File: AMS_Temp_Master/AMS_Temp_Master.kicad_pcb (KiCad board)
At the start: 2 copper layers, 36 parts, among them J1 Conn_01x10_Socket, J2 Conn_01x02_Pin, J3 Conn_01x02_Pin, J4 Conn_01x04_Pin, J5 Conn_01x02_Pin, U1 ATmega328P-A, U2 MCP2515-xSO, U3 MCP2551-I-SN, U4 LD1117S50TR_SOT223, Y1 CSTCE16M0V53-R0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

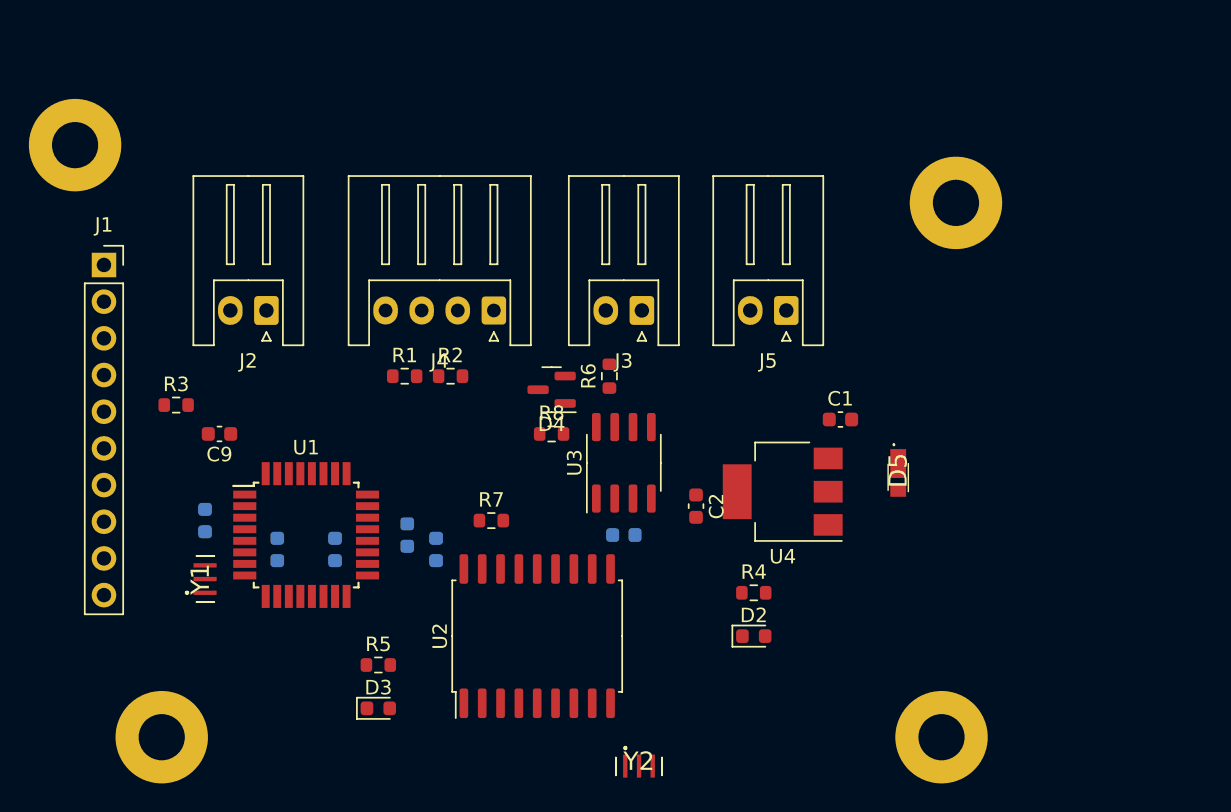
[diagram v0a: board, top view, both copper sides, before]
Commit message: 回路図修正, パターン作成
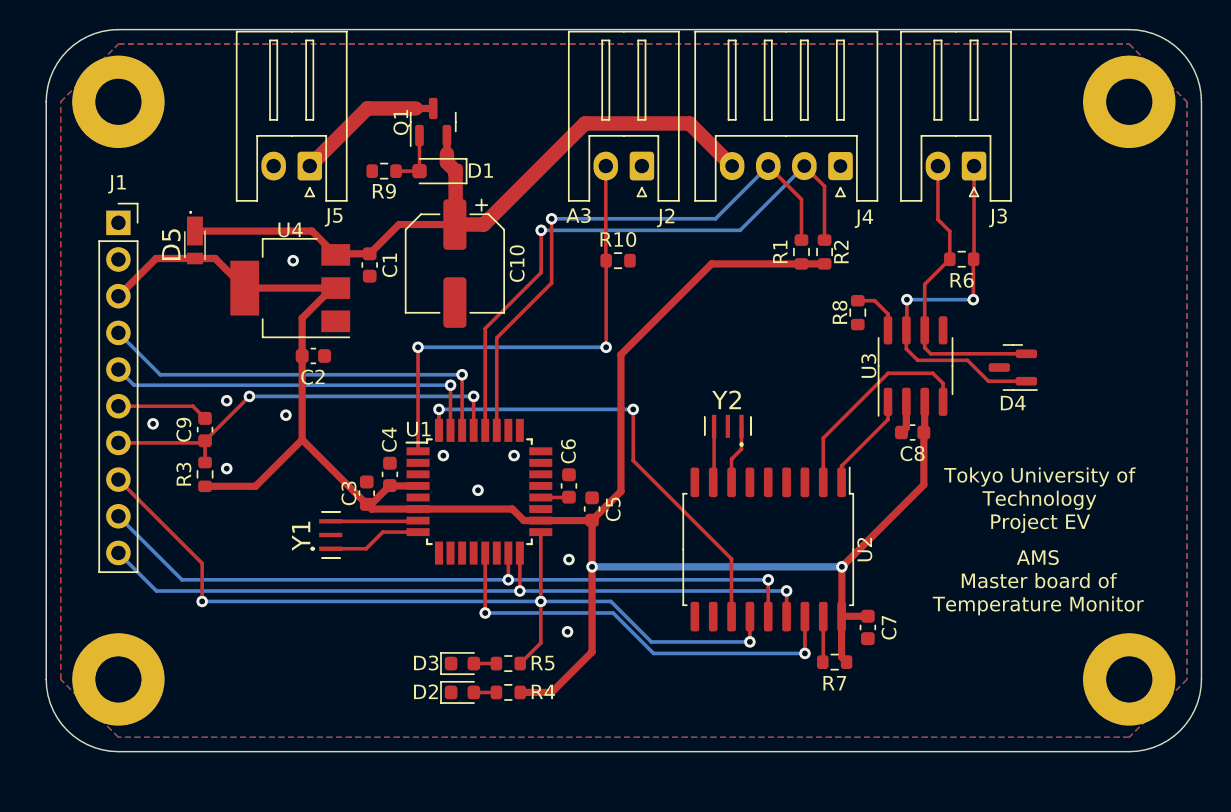
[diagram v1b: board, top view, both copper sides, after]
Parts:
- added C10: 470u, Capacitor_SMD:CP_Elec_6.3x5.4_Nichicon, F.Cu at (138.3, 86.2)
- added D1: UDZV5.1B, Diode_SMD:D_SOD-323_HandSoldering, F.Cu at (137.1, 79.8)
- added Q1: AO3401A, Package_TO_SOT_SMD:SOT-23, F.Cu at (136.8, 76.4)
- added R10: 10k, Resistor_SMD:R_0603_1608Metric, F.Cu at (149.6, 86.0)
- added R9: 10k, Resistor_SMD:R_0603_1608Metric, F.Cu at (133.4, 79.8)
- C3, C4, C5, C6, C7, C8: moved to F.Cu
- moved D5 51.3 mm to (120.3, 84.9)
- moved U4 36.9 mm to (126.9, 87.9)
- moved J5 34.5 mm to (128.2, 79.5)
- moved C1 34.3 mm to (132.4, 86.3), turned to -90 degrees
- moved D4 32.0 mm to (176.9, 93.4)
- moved C7 30.4 mm to (166.9, 111.4), turned to -90 degrees
- moved R1 28.8 mm to (162.3, 85.4), turned to 90 degrees
- moved C2 28.5 mm to (128.5, 92.6), turned to 0 degrees
- moved J2 27.9 mm to (151.2, 79.5)
- moved R2 27.3 mm to (163.9, 85.4), turned to 90 degrees
- moved J4 26.0 mm to (165.0, 79.5)
- moved R7 25.7 mm to (164.6, 113.8), turned to 180 degrees
- moved R6 25.7 mm to (173.4, 85.9), turned to 180 degrees
- moved J3 25.1 mm to (174.2, 79.5)
- moved Y2 24.3 mm to (157.2, 97.5), turned to 0 degrees
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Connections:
- net Net-(J1-Pin_6) renamed /DTR
- net Net-(U1-AREF) renamed /AREF
- net Net-(U1-XTAL1/PB6) renamed /XTAL1
- net Net-(U1-XTAL2/PB7) renamed /XTAL2
- J5 pad 1: +12V -> /+12Vin
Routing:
- net VCC: track 0.00 -> 147.1 mm, vias 0 -> 2
- net /SCK: track 0.00 -> 61.7 mm, vias 0 -> 3
- net /MISO: track 0.00 -> 51.8 mm, vias 0 -> 2
- net /MOSI: track 0.00 -> 51.2 mm, vias 0 -> 2
- net +12V: track 0.00 -> 49.3 mm
- net /SCL: track 0.00 -> 41.2 mm, vias 0 -> 1
- net /SDA: track 0.00 -> 38.8 mm, vias 0 -> 1
- net /AMS_SIG: track 0.00 -> 32.8 mm, vias 0 -> 2
- net /INT: track 0.00 -> 32.1 mm, vias 0 -> 2
- net /CS: track 0.00 -> 30.0 mm, vias 0 -> 2
- net /RESET1: track 0.00 -> 29.8 mm, vias 0 -> 2
- net /RXI: track 0.00 -> 28.9 mm, vias 0 -> 1
- net /TXO: track 0.00 -> 26.6 mm, vias 0 -> 1
- net /CANH: track 0.00 -> 26.5 mm, vias 0 -> 2
- net /CANL: track 0.00 -> 20.9 mm
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- added copper zone on B.Cu, net GND
- added copper zone on F.Cu, net GND
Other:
- board outline added: 80 x 50 mm
- board text added: "A3"
- board text added: "AMS Master board of Temperature Monitor"
- board text added: "Tokyo University of Technology Project EV"

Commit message: パターン作成
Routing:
- net GND: track 2.27 -> 12.6 mm, vias 10 -> 212

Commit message: 修正とパターン完成
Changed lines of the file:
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@@
   (via (at 136.5 90.7) (size 0.8) (drill 0.4) (layers "F.Cu" "B.Cu") (free) (net 2))
   (via (at 153.2 78.2) (size 0.8) (drill 0.4) (layers "F.Cu" "B.Cu") (free) (net 2))
-  (via (at 153.4 100.7) (size 0.8) (drill 0.4) (layers "F.Cu" "B.Cu") (free) (net 2))
+  (via (at 153.6 101.1) (size 0.8) (drill 0.4) (layers "F.Cu" "B.Cu") (free) (net 2))
   (via (at 143 88.1) (size 0.8) (drill 0.4) (layers "F.Cu" "B.Cu") (free) (net 2))
-  (via (at 173.5 94.2) (size 0.8) (drill 0.4) (layers "F.Cu" "B.Cu") (free) (net 2))
+  (via (at 173.4 94.1) (size 0.8) (drill 0.4) (layers "F.Cu" "B.Cu") (free) (net 2))
   (via (at 119.7 102.8) (size 0.8) (drill 0.4) (layers "F.Cu" "B.Cu") (free) (net 2))
   (via (at 148.5 100.9) (size 0.8) (drill 0.4) (layers "F.Cu" "B.Cu") (free) (net 2))
@@
   (via (at 144.1 97.8) (size 0.8) (drill 0.4) (layers "F.Cu" "B.Cu") (free) (net 2))
   (via (at 156.1 118.1) (size 0.8) (drill 0.4) (layers "F.Cu" "B.Cu") (free) (net 2))
-  (via (at 165.1 95.2) (size 0.8) (drill 0.4) (layers "F.Cu" "B.Cu") (free) (net 2))
+  (via (at 164.8 94.8) (size 0.8) (drill 0.4) (layers "F.Cu" "B.Cu") (free) (net 2))
   (via (at 181.9 118.4) (size 0.8) (drill 0.4) (layers "F.Cu" "B.Cu") (free) (net 2))
   (via (at 148.6 94.5) (size 0.8) (drill 0.4) (layers "F.Cu" "B.Cu") (free) (net 2))
@@
   (via (at 116.9 97.4) (size 0.8) (drill 0.4) (layers "F.Cu" "B.Cu") (free) (net 2))
   (via (at 158.8 72) (size 0.8) (drill 0.4) (layers "F.Cu" "B.Cu") (free) (net 2))
-  (via (at 168.1 99.1) (size 0.8) (drill 0.4) (layers "F.Cu" "B.Cu") (free) (net 2))
+  (via (at 168 98.9) (size 0.8) (drill 0.4) (layers "F.Cu" "B.Cu") (free) (net 2))
   (via (at 121.7 87.8) (size 0.8) (drill 0.4) (layers "F.Cu" "B.Cu") (free) (net 2))
   (via (at 183.7 93.5) (size 0.8) (drill 0.4) (layers "F.Cu" "B.Cu") (free) (net 2))
@@
   (segment (start 168.295 95.775) (end 168.295 97.005) (width 0.25) (layer "F.Cu") (net 35))
   (segment (start 168.295 97.005) (end 165.08 100.22) (width 0.25) (layer "F.Cu") (net 35))
-  (segment (start 163.81 98.29) (end 168.3 93.8) (width 0.25) (layer "F.Cu") (net 36))
-  (segment (start 163.81 101.35) (end 163.81 98.29) (width 0.25) (layer "F.Cu") (net 36))
+  (segment (start 167.5 93.8) (end 171.4 93.8) (width 0.25) (layer "F.Cu") (net 36))
   (segment (start 171.4 93.8) (end 172.105 94.505) (width 0.25) (layer "F.Cu") (net 36))
+  (segment (start 163.81 101.35) (end 163.81 97.49) (width 0.25) (layer "F.Cu") (net 36))
+  (segment (start 163.81 97.49) (end 167.5 93.8) (width 0.25) (layer "F.Cu") (net 36))
   (segment (start 172.105 94.505) (end 172.105 95.775) (width 0.25) (layer "F.Cu") (net 36))
-  (segment (start 168.3 93.8) (end 171.4 93.8) (width 0.25) (layer "F.Cu") (net 36))
   (segment (start 157.46 99.14) (end 157.46 101.35) (width 0.25) (layer "F.Cu") (net 41))
   (segment (start 158.15 98.45) (end 157.46 99.14) (width 0.25) (layer "F.Cu") (net 41))

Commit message: modify and complete
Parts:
- moved R8 2.01 mm to (166.4, 91.6)
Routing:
- net /Rs: track 3.61 -> 1.92 mm
- net VCC: track 147.1 -> 145.8 mm
- net GND: track 12.6 -> 12.9 mm, vias 212 -> 187

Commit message: 修正
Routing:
- net GND: vias 187 -> 189
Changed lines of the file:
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@@
   (via (at 149.1 105.8) (size 0.8) (drill 0.4) (layers "F.Cu" "B.Cu") (free) (net 2))
   (via (at 136.5 90.7) (size 0.8) (drill 0.4) (layers "F.Cu" "B.Cu") (free) (net 2))
-  (via (at 153.2 78.9) (size 0.8) (drill 0.4) (layers "F.Cu" "B.Cu") (free) (net 2))
+  (via (at 153.1 78.4) (size 0.8) (drill 0.4) (layers "F.Cu" "B.Cu") (free) (net 2))
   (via (at 153.4 100.7) (size 0.8) (drill 0.4) (layers "F.Cu" "B.Cu") (free) (net 2))
   (via (at 143 88.1) (size 0.8) (drill 0.4) (layers "F.Cu" "B.Cu") (free) (net 2))
@@
   (via (at 144.1 97.8) (size 0.8) (drill 0.4) (layers "F.Cu" "B.Cu") (free) (net 2))
   (via (at 156.1 118.1) (size 0.8) (drill 0.4) (layers "F.Cu" "B.Cu") (free) (net 2))
-  (via (at 164.8 94.8) (size 0.8) (drill 0.4) (layers "F.Cu" "B.Cu") (free) (net 2))
+  (via (at 165.8 93.8) (size 0.8) (drill 0.4) (layers "F.Cu" "B.Cu") (free) (net 2))
   (via (at 148.6 94.5) (size 0.8) (drill 0.4) (layers "F.Cu" "B.Cu") (free) (net 2))
   (via (at 183.6 80.4) (size 0.8) (drill 0.4) (layers "F.Cu" "B.Cu") (free) (net 2))
@@
   (via (at 179.2 73.7) (size 0.8) (drill 0.4) (layers "F.Cu" "B.Cu") (free) (net 2))
   (via (at 155.2 85.1) (size 0.8) (drill 0.4) (layers "F.Cu" "B.Cu") (free) (net 2))
-  (via (at 141.5 80.2) (size 0.8) (drill 0.4) (layers "F.Cu" "B.Cu") (free) (net 2))
+  (via (at 141.4 80.3) (size 0.8) (drill 0.4) (layers "F.Cu" "B.Cu") (free) (net 2))
   (via (at 162.6 99.2) (size 0.8) (drill 0.4) (layers "F.Cu" "B.Cu") (free) (net 2))
   (via (at 147.7 92) (size 0.8) (drill 0.4) (layers "F.Cu" "B.Cu") (free) (net 2))
@@
   (via (at 156.2 75.5) (size 0.8) (drill 0.4) (layers "F.Cu" "B.Cu") (free) (net 2))
   (via (at 153.4 111.2) (size 0.8) (drill 0.4) (layers "F.Cu" "B.Cu") (free) (net 2))
-  (via (at 151.3 110.1) (size 0.8) (drill 0.4) (layers "F.Cu" "B.Cu") (free) (net 2))
+  (via (at 151.7 110.1) (size 0.8) (drill 0.4) (layers "F.Cu" "B.Cu") (free) (net 2))
   (via (at 179.2 91.1) (size 0.8) (drill 0.4) (layers "F.Cu" "B.Cu") (free) (net 2))
   (via (at 150 87.5) (size 0.8) (drill 0.4) (layers "F.Cu" "B.Cu") (free) (net 2))
@@
   (via (at 145.5 95.2) (size 0.8) (drill 0.4) (layers "F.Cu" "B.Cu") (free) (net 2))
   (via (at 136.4 81.4) (size 0.8) (drill 0.4) (layers "F.Cu" "B.Cu") (free) (net 2))
-  (via (at 117 91.2) (size 0.8) (drill 0.4) (layers "F.Cu" "B.Cu") (free) (net 2))
+  (via (at 117.2 91.3) (size 0.8) (drill 0.4) (layers "F.Cu" "B.Cu") (free) (net 2))
   (via (at 126.6 106.7) (size 0.8) (drill 0.4) (layers "F.Cu" "B.Cu") (free) (net 2))
   (via (at 169.4 101) (size 0.8) (drill 0.4) (layers "F.Cu" "B.Cu") (free) (net 2))
@@
   (via (at 161.3 118) (size 0.8) (drill 0.4) (layers "F.Cu" "B.Cu") (free) (net 2))
   (via (at 118.6 71.7) (size 0.8) (drill 0.4) (layers "F.Cu" "B.Cu") (free) (net 2))
-  (via (at 174.6 97.8) (size 0.8) (drill 0.4) (layers "F.Cu" "B.Cu") (free) (net 2))
+  (via (at 173.4 95.7) (size 0.8) (drill 0.4) (layers "F.Cu" "B.Cu") (free) (net 2))
   (via (at 148.3 97.6) (size 0.8) (drill 0.4) (layers "F.Cu" "B.Cu") (free) (net 2))
   (via (at 161 95.2) (size 0.8) (drill 0.4) (layers "F.Cu" "B.Cu") (free) (net 2))
@@
   (via (at 148.4 114.6) (size 0.8) (drill 0.4) (layers "F.Cu" "B.Cu") (free) (net 2))
   (via (at 166.6 109.1) (size 0.8) (drill 0.4) (layers "F.Cu" "B.Cu") (free) (net 2))
-  (via (at 134.4 78.1) (size 0.8) (drill 0.4) (layers "F.Cu" "B.Cu") (free) (net 2))
+  (via (at 134.5 78.3) (size 0.8) (drill 0.4) (layers "F.Cu" "B.Cu") (free) (net 2))
   (via (at 160.7 84.8) (size 0.8) (drill 0.4) (layers "F.Cu" "B.Cu") (free) (net 2))
   (via (at 152.7 71.8) (size 0.8) (drill 0.4) (layers "F.Cu" "B.Cu") (free) (net 2))
@@
   (via (at 140.3 89) (size 0.8) (drill 0.4) (layers "F.Cu" "B.Cu") (free) (net 2))
   (via (at 187.9 99.7) (size 0.8) (drill 0.4) (layers "F.Cu" "B.Cu") (free) (net 2))
-  (via (at 121.5 90.7) (size 0.8) (drill 0.4) (layers "F.Cu" "B.Cu") (free) (net 2))
+  (via (at 121.9 90.5) (size 0.8) (drill 0.4) (layers "F.Cu" "B.Cu") (free) (net 2))
   (via (at 183.6 89.3) (size 0.8) (drill 0.4) (layers "F.Cu" "B.Cu") (free) (net 2))
   (via (at 119.2 110.2) (size 0.8) (drill 0.4) (layers "F.Cu" "B.Cu") (free) (net 2))
@@
   (via (at 118.7 118.3) (size 0.8) (drill 0.4) (layers "F.Cu" "B.Cu") (free) (net 2))
   (via (at 167.33 113.93) (size 0.8) (drill 0.4) (layers "F.Cu" "B.Cu") (free) (net 2))
+  (via (at 152 103) (size 0.8) (drill 0.4) (layers "F.Cu" "B.Cu") (free) (net 2))
   (via (at 176.1 81.1) (size 0.8) (drill 0.4) (layers "F.Cu" "B.Cu") (free) (net 2))
   (via (at 146.3 88.9) (size 0.8) (drill 0.4) (layers "F.Cu" "B.Cu") (free) (net 2))
@@
   (via (at 117.1 84.6) (size 0.8) (drill 0.4) (layers "F.Cu" "B.Cu") (free) (net 2))
   (via (at 174.4 113.2) (size 0.8) (drill 0.4) (layers "F.Cu" "B.Cu") (free) (net 2))
-  (via (at 118 87.3) (size 0.8) (drill 0.4) (layers "F.Cu" "B.Cu") (free) (net 2))
+  (via (at 118 87.4) (size 0.8) (drill 0.4) (layers "F.Cu" "B.Cu") (free) (net 2))
   (via (at 129.6 75.3) (size 0.8) (drill 0.4) (layers "F.Cu" "B.Cu") (free) (net 2))
   (via (at 155 99.2) (size 0.8) (drill 0.4) (layers "F.Cu" "B.Cu") (free) (net 2))
@@
   (via (at 143.5 82.6) (size 0.8) (drill 0.4) (layers "F.Cu" "B.Cu") (free) (net 2))
   (via (at 131.9 81.3) (size 0.8) (drill 0.4) (layers "F.Cu" "B.Cu") (free) (net 2))
-  (via (at 172.3 97.8) (size 0.8) (drill 0.4) (layers "F.Cu" "B.Cu") (free) (net 2))
+  (via (at 172.2 98.9) (size 0.8) (drill 0.4) (layers "F.Cu" "B.Cu") (free) (net 2))
   (via (at 183.6 106.7) (size 0.8) (drill 0.4) (layers "F.Cu" "B.Cu") (free) (net 2))
   (via (at 137.6 99.6) (size 0.8) (drill 0.4) (layers "F.Cu" "B.Cu") (free) (net 2))
@@
   (via (at 158.5 91.7) (size 0.8) (drill 0.4) (layers "F.Cu" "B.Cu") (free) (net 2))
   (via (at 187.9 91.4) (size 0.8) (drill 0.4) (layers "F.Cu" "B.Cu") (free) (net 2))
-  (via (at 117 104) (size 0.8) (drill 0.4) (layers "F.Cu" "B.Cu") (free) (net 2))
-  (via (at 155.7 81.1) (size 0.8) (drill 0.4) (layers "F.Cu" "B.Cu") (free) (net 2))
+  (via (at 117.2 104) (size 0.8) (drill 0.4) (layers "F.Cu" "B.Cu") (free) (net 2))
+  (via (at 155.6 81.3) (size 0.8) (drill 0.4) (layers "F.Cu" "B.Cu") (free) (net 2))
   (via (at 126.4 96.6) (size 0.8) (drill 0.4) (layers "F.Cu" "B.Cu") (free) (net 2))
-  (via (at 119.6 106.7) (size 0.8) (drill 0.4) (layers "F.Cu" "B.Cu") (free) (net 2))
+  (via (at 119.6 106.5) (size 0.8) (drill 0.4) (layers "F.Cu" "B.Cu") (free) (net 2))
   (via (at 150 74.6) (size 0.8) (drill 0.4) (layers "F.Cu" "B.Cu") (free) (net 2))
   (via (at 161.3 76.3) (size 0.8) (drill 0.4) (layers "F.Cu" "B.Cu") (free) (net 2))
+  (via (at 151 89.4) (size 0.8) (drill 0.4) (layers "F.Cu" "B.Cu") (free) (net 2))
   (via (at 122.1 106.8) (size 0.8) (drill 0.4) (layers "F.Cu" "B.Cu") (free) (net 2))
   (via (at 166.9 81.1) (size 0.8) (drill 0.4) (layers "F.Cu" "B.Cu") (free) (net 2))
   (via (at 119.3 114.4) (size 0.8) (drill 0.4) (layers "F.Cu" "B.Cu") (free) (net 2))
   (via (at 158.8 72) (size 0.8) (drill 0.4) (layers "F.Cu" "B.Cu") (free) (net 2))
-  (via (at 168 99.8) (size 0.8) (drill 0.4) (layers "F.Cu" "B.Cu") (free) (net 2))
-  (via (at 121.7 87.8) (size 0.8) (drill 0.4) (layers "F.Cu" "B.Cu") (free) (net 2))
+  (via (at 167.5 99.4) (size 0.8) (drill 0.4) (layers "F.Cu" "B.Cu") (free) (net 2))
+  (via (at 121.5 88) (size 0.8) (drill 0.4) (layers "F.Cu" "B.Cu") (free) (net 2))
   (via (at 183.7 93.5) (size 0.8) (drill 0.4) (layers "F.Cu" "B.Cu") (free) (net 2))
-  (via (at 162.4 114.7) (size 0.8) (drill 0.4) (layers "F.Cu" "B.Cu") (free) (net 2))
+  (via (at 162.1 114.8) (size 0.8) (drill 0.4) (layers "F.Cu" "B.Cu") (free) (net 2))
   (via (at 163.8 72.2) (size 0.8) (drill 0.4) (layers "F.Cu" "B.Cu") (free) (net 2))
   (via (at 172.7 102.1) (size 0.8) (drill 0.4) (layers "F.Cu" "B.Cu") (free) (net 2))

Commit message: 完成, 発注
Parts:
- moved R10 3.20 mm to (149.6, 89.2)
- moved Y1 2.46 mm to (131.9, 106.1), turned to 0 degrees
- moved D5 2.06 mm to (120.5, 87.0)
- moved C3 1.38 mm to (133.0, 103.2), turned to 180 degrees
- moved R3 1.13 mm to (122.1, 100.5)
- moved C9 1.12 mm to (122.1, 97.5)
- moved R6 0.60 mm to (173.5, 86.5)
- moved Y2 0.32 mm to (156.9, 97.6)
- moved C8 0.10 mm to (170.0, 97.8)
- moved J2 0.05 mm to (151.3, 79.5)
- moved J3 0.05 mm to (174.3, 79.5)
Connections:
- REF** pad 1: (no net) -> GND (x4)
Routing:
- net +12V: track 49.0 -> 52.4 mm
- net /INT: track 32.1 -> 34.7 mm
- net /XTAL2: track 6.53 -> 3.99 mm
- net /SCK: track 62.1 -> 64.5 mm
- net VCC: track 145.8 -> 143.5 mm
- net /AMS_SIG: track 32.8 -> 31.5 mm
- net /+12Vin: track 10.2 -> 11.4 mm
- net /RESET1: track 29.8 -> 30.9 mm
- net /DTR: track 6.35 -> 7.36 mm
- net GND: track 12.9 -> 13.9 mm, vias 189 -> 187
- net /TXCAN: track 6.91 -> 7.71 mm
- net /CANL: track 20.9 -> 21.5 mm
- net /RXCAN: track 15.2 -> 14.7 mm
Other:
- board text added: "12V"
- board text added: "AMS_SIG"
- board text added: "CANH"
- board text added: "CANL"
- board text added: "CTS"
- board text added: "DTR"
- board text added: "GND"
- board text added: "MISO"
- board text added: "MOSI"
- board text added: "RESET"
- board text added: "RXI"
- board text added: "SCK"
- board text added: "SCL"
- board text added: "SDA"
- board text added: "TXO"
- board text added: "VCC"

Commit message: 10k抵抗フットプリント修正2012
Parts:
- R10, R3, R7, R9: footprint Resistor_SMD:R_0603_1608Metric -> Resistor_SMD:R_0805_2012Metric
- moved R7 0.32 mm to (164.7, 114.1)
- moved R3 0.26 mm to (122.1, 100.8)
- moved R10 0.22 mm to (149.7, 89.0)
- moved R9 0.10 mm to (133.3, 79.8)
